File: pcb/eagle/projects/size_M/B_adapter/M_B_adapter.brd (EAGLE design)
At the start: 6 parts

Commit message: PCB M.1
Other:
- board text added: "PA3"
- board text added: "PA6"
- board text added: "PA7"
- board text added: "adapter M.1"
- board text removed: "P0"
- board text removed: "P1"
- board text removed: "P4"
- board text removed: "base M.1"
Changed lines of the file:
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@@
 <wire x1="21" y1="21" x2="21" y2="0" width="0.2" layer="48"/>
 <wire x1="21" y1="0" x2="0" y2="0" width="0.2" layer="48"/>
-<hole x="2" y="2" drill="2.1"/>
+<hole x="2" y="2" drill="1.6"/>
 <text x="3.8956" y="9.247" size="1.143" layer="22" rot="MR315" align="center">SDA</text>
 <text x="3.9718" y="6.58" size="1.143" layer="22" rot="MR315" align="center">SCL</text>
@@
 <text x="17.3308" y="6.6026" size="1.143" layer="22" rot="MR315" align="center">GND</text>
 <text x="17.4324" y="9.295" size="1.143" layer="22" rot="MR315" align="center">3V3</text>
-<text x="3.7164" y="14.3924" size="1.143" layer="22" rot="MR315" align="center">P0</text>
-<text x="3.7672" y="11.8524" size="1.143" layer="22" rot="MR315" align="center">P1</text>
-<text x="3.6416" y="16.9258" size="1.143" layer="22" rot="MR315" align="center">P4</text>
+<text x="3.7164" y="14.3924" size="1.143" layer="22" rot="MR315" align="center">PA6</text>
+<text x="3.7672" y="11.8524" size="1.143" layer="22" rot="MR315" align="center">PA7</text>
+<text x="3.6416" y="16.9258" size="1.143" layer="22" rot="MR315" align="center">PA3</text>
 <circle x="2" y="2" radius="1.9" width="0.1" layer="52"/>
-<hole x="19" y="19" drill="2.1"/>
+<hole x="19" y="19" drill="1.6"/>
 <circle x="19" y="19" radius="1.9" width="0.1" layer="52"/>
-<text x="10.2984" y="3.873" size="1.6764" layer="22" rot="MR0" align="center">base M.1</text>
+<text x="11.0604" y="1.6632" size="1.6764" layer="22" rot="MR0" align="center">adapter M.1</text>
 <text x="17.1276" y="11.454" size="1.143" layer="22" rot="MR315" align="center">VBAT</text>
 <text x="16.9498" y="14.0702" size="1.143" layer="22" rot="MR315" align="center">VUSB</text>
@@
 <wire x1="5.00229375" y1="19.3722" x2="4.98009375" y2="19.35" width="0.6096" layer="1"/>
 <wire x1="4.98009375" y1="19.35" x2="1.4" y2="19.39" width="0.6096" layer="1"/>
-<wire x1="14.2084" y1="14.31" x2="9.1462" y2="19.3722" width="0.6096" layer="1"/>
-<wire x1="9.1462" y1="19.3722" x2="7.4676" y2="19.3722" width="0.6096" layer="1"/>
 <wire x1="7.4676" y1="19.3722" x2="5.00229375" y2="19.3722" width="0.6096" layer="1"/>
 <wire x1="7.5048" y1="18.2626" x2="7.4676" y2="18.2998" width="0.3556" layer="1"/>
@@
 <wire x1="6.6848" y1="5.35845625" x2="6.6848" y2="6.6848" width="0.6096" layer="16"/>
 <wire x1="6.6848" y1="6.6848" x2="6.69" y2="6.69" width="0.6096" layer="16"/>
-<wire x1="14.2084" y1="14.31" x2="14.31" y2="14.31" width="0" layer="19" extent="1-1"/>
+<wire x1="9.2478" y1="19.3722" x2="14.31" y2="14.31" width="0.6096" layer="1"/>
+<wire x1="7.4676" y1="19.3722" x2="9.2478" y2="19.3722" width="0.6096" layer="1"/>
 </signal>
 <signal name="3V3">

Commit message: closed PCB version M.2
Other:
- board text added: "adapter M.2"
- board text removed: "adapter M.1"
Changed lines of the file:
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@@
 <setting verticaltext="up"/>
 </settings>
-<grid distance="1" unitdist="mil" unit="mm" style="lines" multiple="1" display="yes" altdistance="0.1" altunitdist="mm" altunit="mm"/>
+<grid distance="0.5" unitdist="mm" unit="mm" style="lines" multiple="1" display="yes" altdistance="0.1" altunitdist="mm" altunit="mm"/>
 <layers>
 <layer number="1" name="Top" color="4" fill="1" visible="yes" active="yes"/>
@@
 <layer number="56" name="wert" color="7" fill="1" visible="no" active="no"/>
 <layer number="57" name="tCAD" color="7" fill="1" visible="no" active="no"/>
+<layer number="59" name="tCarbon" color="7" fill="1" visible="no" active="no"/>
+<layer number="60" name="bCarbon" color="7" fill="1" visible="no" active="no"/>
 <layer number="88" name="SimResults" color="9" fill="1" visible="no" active="no"/>
 <layer number="89" name="SimProbes" color="9" fill="1" visible="no" active="no"/>
@@
 <layer number="112" name="tSilk" color="7" fill="1" visible="yes" active="yes"/>
 <layer number="113" name="ReferenceLS" color="7" fill="1" visible="no" active="no"/>
+<layer number="114" name="Badge_Outline" color="7" fill="1" visible="no" active="yes"/>
+<layer number="115" name="ReferenceISLANDS" color="7" fill="1" visible="no" active="yes"/>
 <layer number="116" name="centerDrill" color="7" fill="1" visible="yes" active="yes"/>
 <layer number="118" name="Rect_Pads" color="7" fill="1" visible="no" active="no"/>
@@
 <layer number="127" name="_tValues" color="7" fill="1" visible="yes" active="yes"/>
 <layer number="128" name="_bValues" color="7" fill="1" visible="yes" active="yes"/>
+<layer number="129" name="Mask" color="7" fill="1" visible="no" active="yes"/>
 <layer number="131" name="tAdjust" color="7" fill="1" visible="yes" active="yes"/>
 <layer number="132" name="bAdjust" color="7" fill="1" visible="yes" active="yes"/>
@@
 <layer number="223" name="223bmp" color="24" fill="1" visible="no" active="no"/>
 <layer number="224" name="224bmp" color="25" fill="1" visible="no" active="no"/>
+<layer number="225" name="225bmp" color="7" fill="1" visible="no" active="yes"/>
+<layer number="226" name="226bmp" color="7" fill="1" visible="no" active="yes"/>
+<layer number="227" name="227bmp" color="7" fill="1" visible="no" active="yes"/>
+<layer number="228" name="228bmp" color="7" fill="1" visible="no" active="yes"/>
+<layer number="229" name="229bmp" color="7" fill="1" visible="no" active="yes"/>
+<layer number="230" name="230bmp" color="7" fill="1" visible="no" active="yes"/>
 <layer number="231" name="Eagle3D_PG1" color="7" fill="1" visible="no" active="no"/>
 <layer number="232" name="Eagle3D_PG2" color="7" fill="1" visible="no" active="no"/>
@@
 <layer number="251" name="SMDround" color="7" fill="1" visible="no" active="no"/>
 <layer number="254" name="cooling" color="7" fill="1" visible="yes" active="yes"/>
+<layer number="255" name="routoute" color="7" fill="1" visible="no" active="yes"/>
 </layers>
 <board>
@@
 <hole x="19" y="19" drill="1.6"/>
 <circle x="19" y="19" radius="1.9" width="0.1" layer="52"/>
-<text x="11.0604" y="1.6632" size="1.6764" layer="22" rot="MR0" align="center">adapter M.1</text>
+<text x="11.0604" y="1.6632" size="1.6764" layer="22" rot="MR0" align="center">adapter M.2</text>
 <text x="17.1276" y="11.454" size="1.143" layer="22" rot="MR315" align="center">VBAT</text>
 <text x="16.9498" y="14.0702" size="1.143" layer="22" rot="MR315" align="center">VUSB</text>
@@
 <rectangle x1="11.5697" y1="9.2329" x2="14.3383" y2="9.2583" layer="22" rot="R180"/>
 <rectangle x1="11.6713" y1="9.2583" x2="14.2367" y2="9.2837" layer="22" rot="R180"/>
+<circle x="19" y="19" radius="1" width="0.254" layer="41"/>
+<circle x="19" y="19" radius="1" width="0.254" layer="42"/>
+<circle x="2" y="2" radius="1" width="0.254" layer="42"/>
+<circle x="2" y="2" radius="1" width="0.254" layer="41"/>
 </plain>
 <attributes>

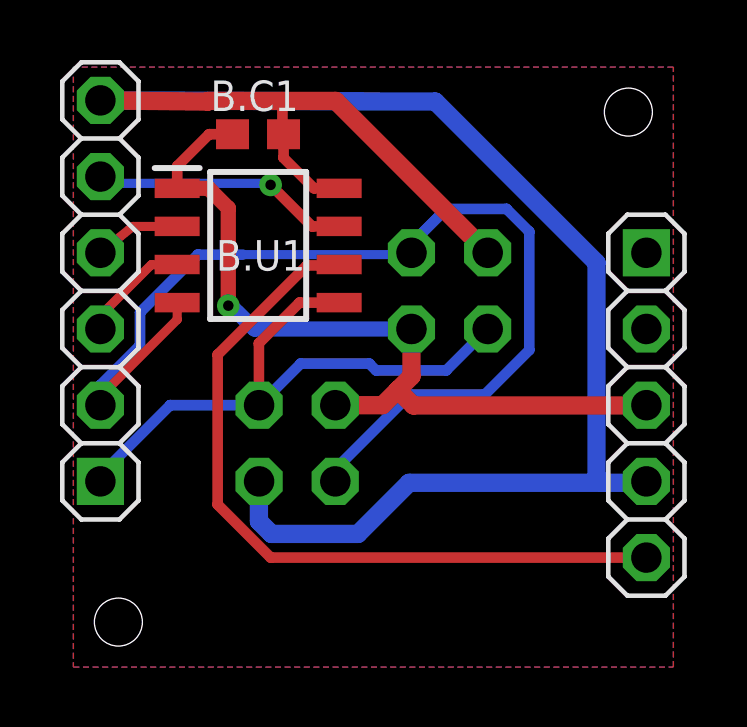
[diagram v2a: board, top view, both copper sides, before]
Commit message: pull-up resistors for i2c
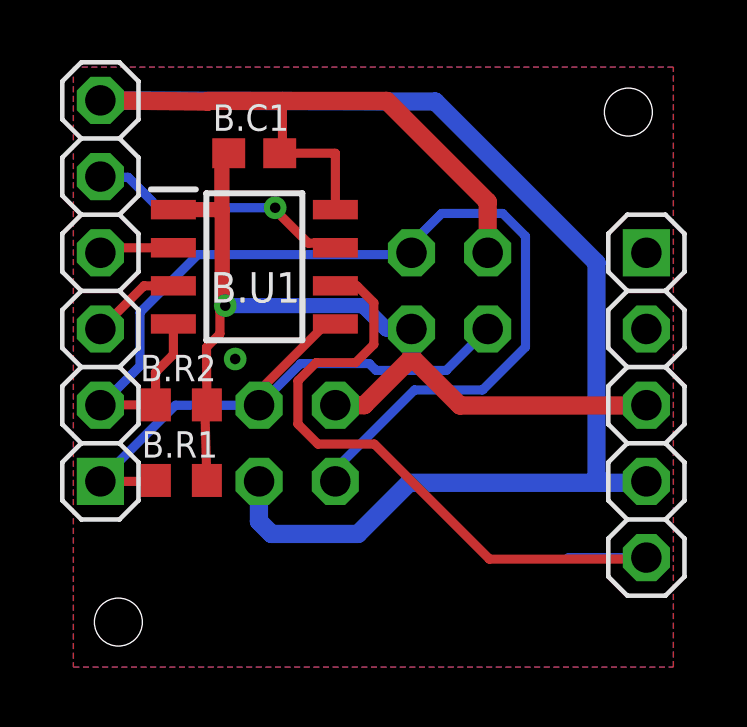
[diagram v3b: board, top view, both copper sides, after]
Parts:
- added B.R1, B.R2: alt 2k2 for master, rcl:R0603
- moved B.U1 0.72 mm to (6.53, 13.8)
- moved B.C1 0.65 mm to (6.53, 17.6)
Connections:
- net 3V3: now also B.R1.2, B.R2.2
- net SCL: now also B.R1.1
- net SDA: now also B.R2.1
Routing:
- net 3V3: track 27.7 -> 34.2 mm
- net UPDI: track 27.9 -> 23.5 mm
- net GND: track 60.6 -> 62.9 mm, vias 0 -> 1
- net PA7: track 3.79 -> 3.10 mm
- added copper zone on layer 1, net GND
- removed copper zone on layer 1, net 3V3
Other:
- board text added: "adapter M.6"
- board text removed: "adapter M.2"

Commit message: minor changes for PCB v6.
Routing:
- net UPDI: track 23.5 -> 20.9 mm
- net SDA: track 35.3 -> 34.6 mm
- net GND: vias 1 -> 2
